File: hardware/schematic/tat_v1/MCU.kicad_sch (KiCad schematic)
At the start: 23 parts, among them J3 JST-SH 1x7P, SW2 SW_SPDT, SW3 SW_Push, U4 STM32U073CCUx, X1 32.768KHz

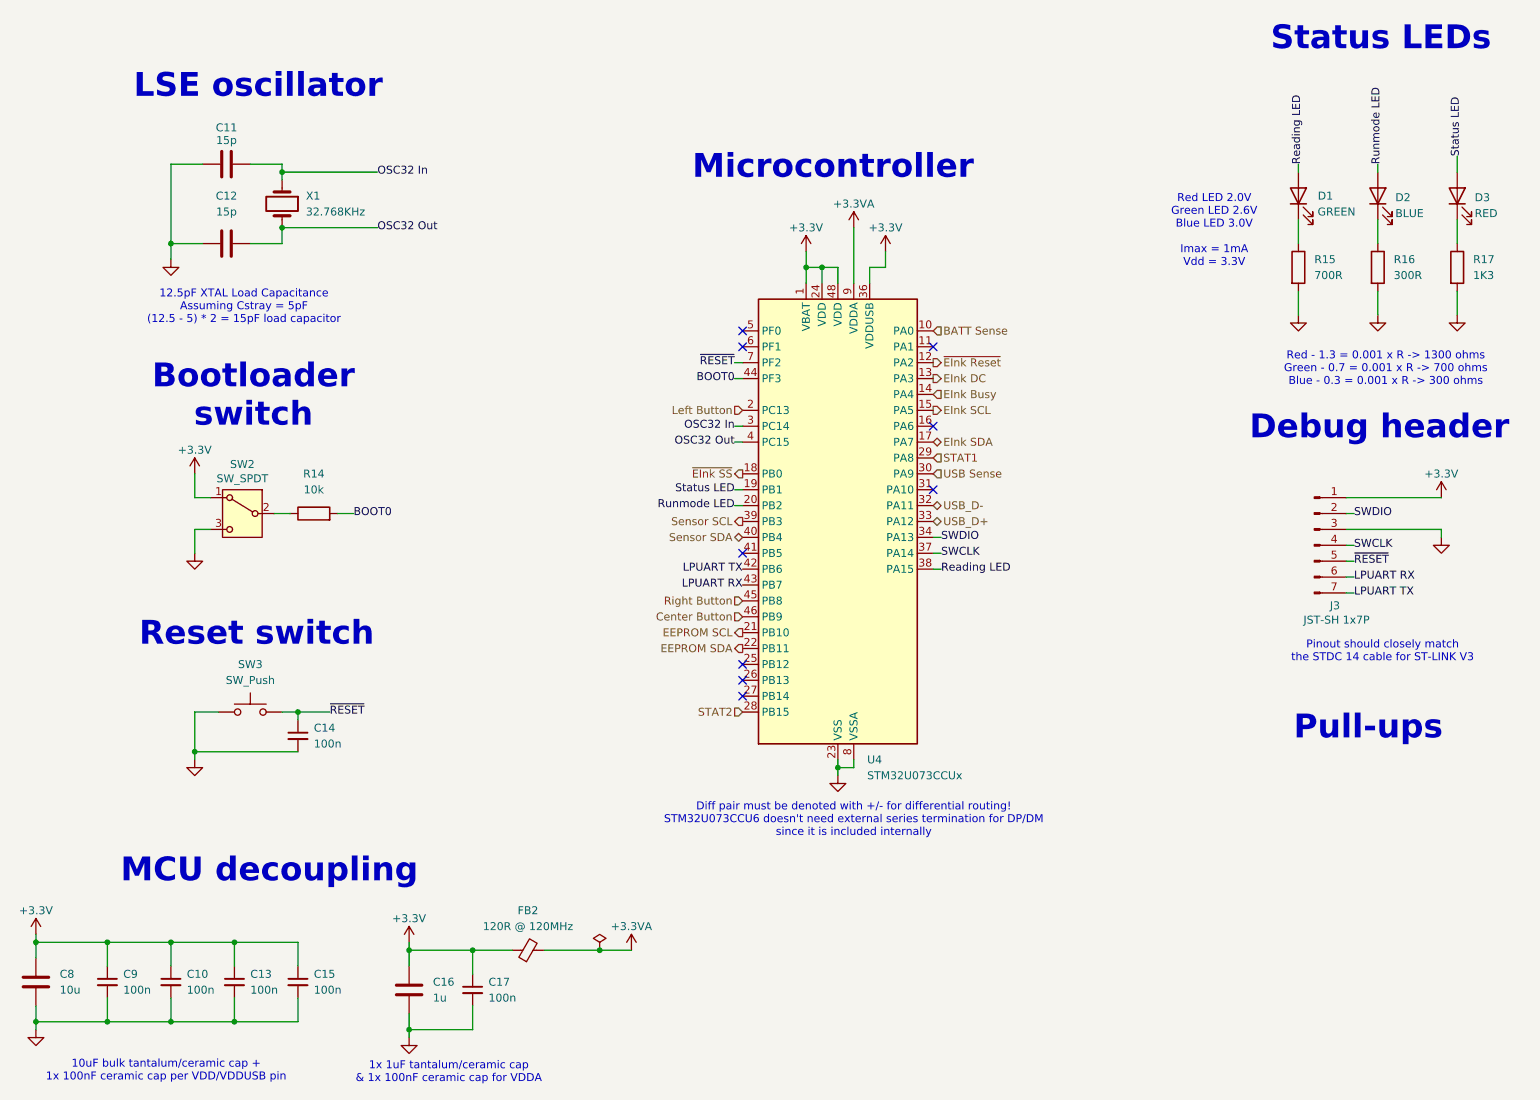
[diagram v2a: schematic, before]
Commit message: Most simple footprints added. Need to create footprints for more complex parts.
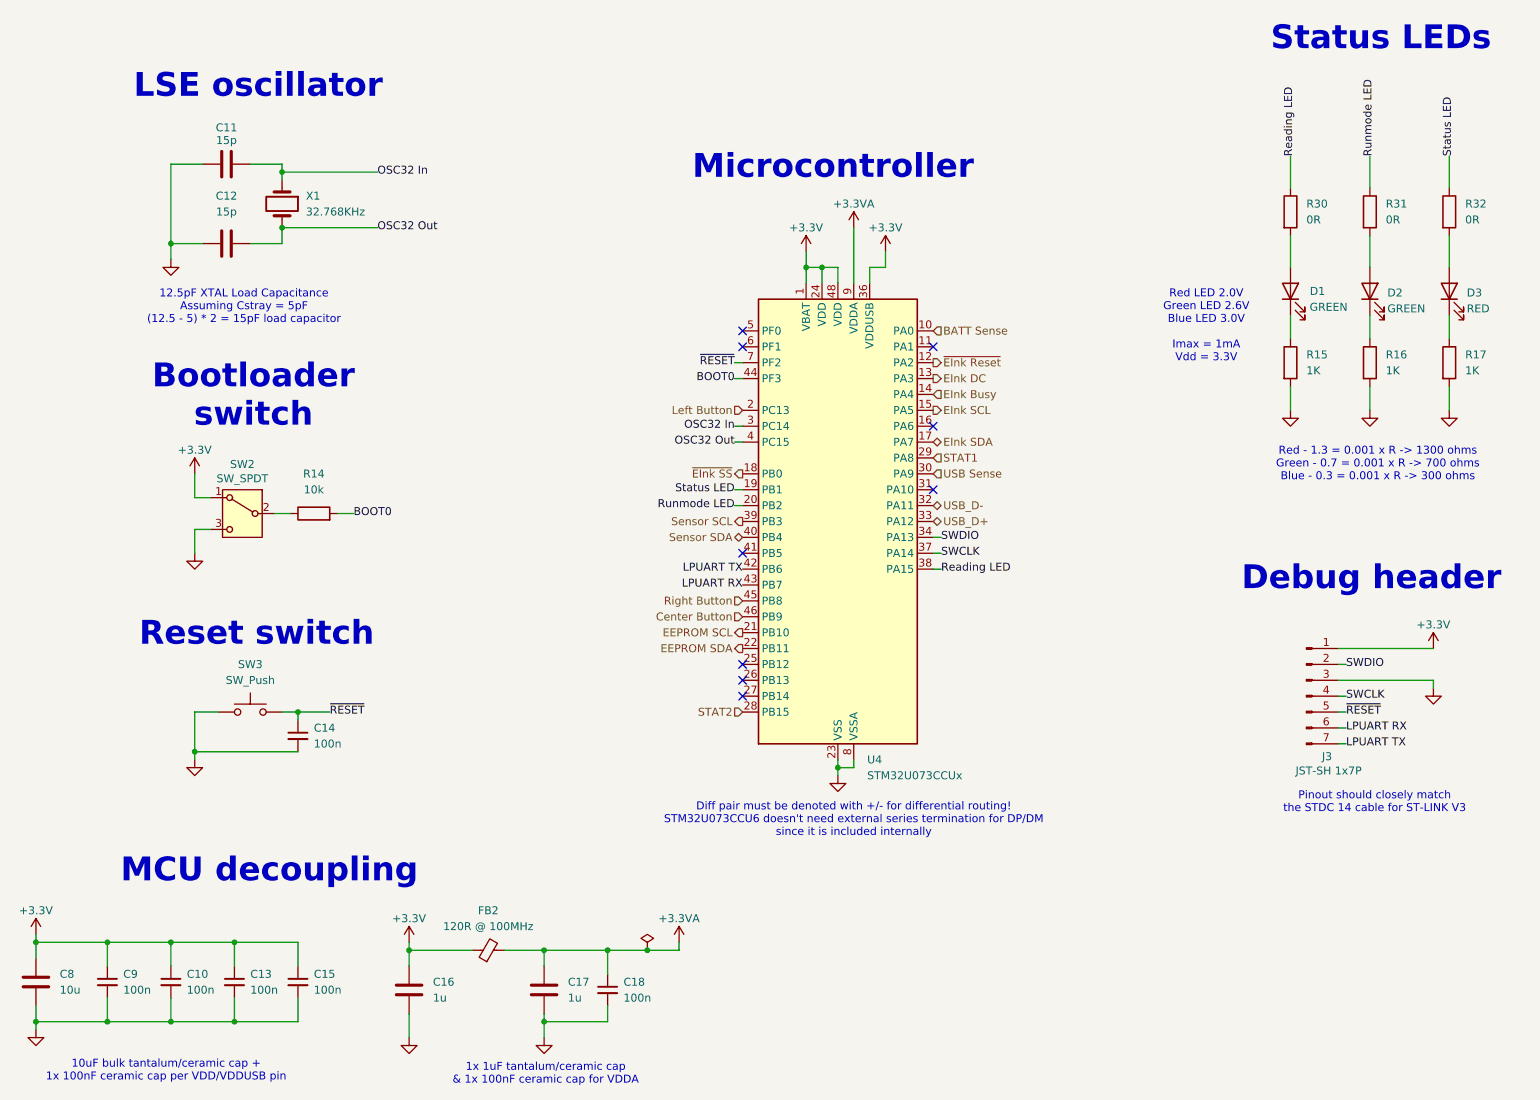
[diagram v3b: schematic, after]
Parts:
- added C16: 1u, symbol Device:C
- added R30, R31, R32: 0R, Jumper:SolderJumper-2_P1.3mm_Bridged2Bar_RoundedPad1.0x1.5mm, symbol Device:R
- C10, C11, C12, C13, C14, C15, C8, C9: Link (none) -> https://www.lcsc.com/product-detail/Multilayer-Ceramic-Capa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
- C17: renamed from C16; Link (none) -> https://www.lcsc.com/product-detail/Multilayer-Ceramic-Capa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
- C18: renamed from C17; Link (none) -> https://www.lcsc.com/product-detail/Multilayer-Ceramic-Capa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
- D1, D3: footprint (none) -> LED_SMD:LED_0603_1608Metric; Link (none) -> https://www.lcsc.com/product-detail/LED-Indication-Discrete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
- D2: value BLUE -> GREEN; footprint (none) -> LED_SMD:LED_0603_1608Metric; Link (none) -> https://www.lcsc.com/product-detail/LED-Indication-Discrete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
- FB2: value 120R @ 120MHz -> 120R @ 100MHz; footprint (none) -> Inductor_SMD:L_0603_1608Metric; Link (none) -> https://www.lcsc.com/product-detail/Ferrite-Beads_Murata-El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
- J3: footprint (none) -> Connector_JST:JST_SH_SM07B-SRSS-TB_1x07-1MP_P1.00mm_Horizontal; Link (none) -> https://www.lcsc.com/product-detail/Wire-To-Board-Connector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
- R15: value 700R -> 1K; footprint Resistor_SMD:R_0402_1005Metric -> Resistor_SMD:R_0603_1608Metric; Link (none) -> https://www.lcsc.com/product-detail/Chip-Resistor-Surface-M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
- R16: value 300R -> 1K; footprint Resistor_SMD:R_0402_1005Metric -> Resistor_SMD:R_0603_1608Metric; Link (none) -> https://www.lcsc.com/product-detail/Chip-Resistor-Surface-M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
- R17: value 1K3 -> 1K; footprint Resistor_SMD:R_0402_1005Metric -> Resistor_SMD:R_0603_1608Metric; Link (none) -> https://www.lcsc.com/product-detail/Chip-Resistor-Surface-M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
- SW3: footprint (none) -> Button_Switch_SMD:SW_Push_1P1T_XKB_TS-1187A
- X1: footprint (none) -> Crystal:Crystal_SMD_3215-2Pin_3.2x1.5mm; Link (none) -> https://www.lcsc.com/product-detail/Crystals_Seiko-Epson-Q1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
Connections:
- net +3.3V: now also C16.1; no longer C17.1, C18.1
- net +3.3VA: now also C17.1, C18.1
- net GND: now also C16.2
- net Reading LED: now also R30.1; no longer D1.2 (A)
- net Runmode LED: now also R31.1; no longer D2.2 (A)
- net Status LED: now also R32.1; no longer D3.2 (A)
- new net: D3.2 (A), R32.2
- new net: D2.2 (A), R31.2
- new net: D1.2 (A), R30.2
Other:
- note removed: "Pull-ups"
- moved on the sheet: C17, C18, D1, D2, D3, FB2, J3, R15, R16, R17

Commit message: Finished all footprints, can now start laying out circuit
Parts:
- C10, C13, C15, C18, C9: footprint (none) -> Capacitor_SMD:C_0402_1005Metric
- C16, C17: footprint (none) -> Capacitor_SMD:C_0603_1608Metric
- C8: footprint (none) -> Capacitor_SMD:C_0805_2012Metric
- SW2: footprint (none) -> tat_footprints:SW_SPDT_HANXIA_Mini_MSK12CO2
- SW3: footprint Button_Switch_SMD:SW_Push_1P1T_XKB_TS-1187A -> tat_footprints:SW_Push_SHOU_HAN_SPST_TS3425BA; Link (none) -> https://www.lcsc.com/product-detail/Tactile-Switches_XUNPU-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
- renumbered R30 to R15, R15 to R16, R31 to R17, R16 to R18, R32 to R19, R17 to R20
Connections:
- net +3.3V: now also SW2.3 (C); no longer SW2.1 (A)
- net GND: now also SW2.1 (A); no longer SW2.3 (C)
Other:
- moved on the sheet: SW2
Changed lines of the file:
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@@
 	(wire
 		(pts
-			(xy 50.8 93.98) (xy 53.34 93.98)
-		)
-		(stroke
-			(width 0)
-			(type default)
-		)
-	)
-	(wire
-		(pts
 			(xy 116.84 177.8) (xy 106.68 177.8)
 		)
@@
 	(wire
 		(pts
+			(xy 63.5 96.52) (xy 66.04 96.52)
+		)
+		(stroke
+			(width 0)
+			(type default)
+		)
+	)
+	(wire
+		(pts
 			(xy 251.46 76.2) (xy 251.46 80.01)
 		)
@@
 	(wire
 		(pts
+			(xy 50.8 93.98) (xy 53.34 93.98)
+		)
+		(stroke
+			(width 0)
+			(type default)
+		)
+	)
+	(wire
+		(pts
 			(xy 161.29 57.15) (xy 158.75 57.15)
 		)
@@
 	(wire
 		(pts
-			(xy 25.4 165.1) (xy 25.4 167.64)
+			(xy 50.8 99.06) (xy 53.34 99.06)
 		)
 		(stroke
@@
 	(wire
 		(pts
-			(xy 57.15 173.99) (xy 57.15 177.8)
-		)
-		(stroke
-			(width 0)
-			(type default)
-		)
-	)
-	(wire
-		(pts
-			(xy 233.68 130.81) (xy 234.95 130.81)
+			(xy 25.4 165.1) (xy 25.4 167.64)
 		)
 		(stroke
@@
 	(wire
 		(pts
-			(xy 170.18 102.87) (xy 168.91 102.87)
+			(xy 57.15 173.99) (xy 57.15 177.8)
 		)
 		(stroke
@@
 	(wire
 		(pts
-			(xy 25.4 163.83) (xy 25.4 165.1)
+			(xy 233.68 130.81) (xy 234.95 130.81)
 		)
 		(stroke
@@
 	(wire
 		(pts
-			(xy 85.09 165.1) (xy 85.09 166.37)
+			(xy 170.18 102.87) (xy 168.91 102.87)
 		)
 		(stroke
@@
 	(wire
 		(pts
-			(xy 50.8 90.17) (xy 50.8 93.98)
+			(xy 25.4 163.83) (xy 25.4 165.1)
 		)
 		(stroke
@@
 	(wire
 		(pts
-			(xy 53.34 99.06) (xy 50.8 99.06)
+			(xy 85.09 165.1) (xy 85.09 166.37)
 		)
 		(stroke
@@
 	(wire
 		(pts
-			(xy 63.5 96.52) (xy 66.04 96.52)
+			(xy 50.8 90.17) (xy 50.8 93.98)
 		)
 		(stroke
@@
 			)
 		)
-		(property "Footprint" ""
+		(property "Footprint" "Capacitor_SMD:C_0402_1005Metric"
 			(at 116.84 172.72 0)
 			(effects
@@
 	(symbol
 		(lib_id "Switch:SW_SPDT")
-		(at 58.42 96.52 0)
-		(mirror y)
+		(at 58.42 96.52 180)
 		(unit 1)
 		(exclude_from_sim no)
@@
 		(dnp no)
 		(property "Reference" "SW2"
-			(at 58.42 88.646 0)
+			(at 58.42 104.394 0)
 			(effects
 				(font
@@
 		)
 		(property "Value" "SW_SPDT"
-			(at 58.42 90.932 0)
+			(at 58.42 102.108 0)
 			(effects
 				(font
@@
 			)
 		)
-		(property "Footprint" ""
+		(property "Footprint" "tat_footprints:SW_SPDT_HANXIA_Mini_MSK12CO2"
 			(at 58.42 96.52 0)
 			(effects
@@
 		)
 		(property "Datasheet" "~"
-			(at 58.42 104.14 0)
+			(at 58.42 88.9 0)
 			(effects
 				(font
@@
 		(dnp no)
 		(fields_autoplaced yes)
-		(property "Reference" "R15"
+		(property "Reference" "R16"
 			(at 228.6 71.1199 0)
 			(effects
@@
 			(project "tat_v1"
 				(path "/b6d2ddf1-6792-45dd-afc9-29fd74d587ec/61278459-0872-433c-8091-dd4d841ee895"
-					(reference "R15")
+					(reference "R16")
 					(unit 1)
 				)
@@
 			)
 		)
-		(property "Footprint" ""
+		(property "Footprint" "Capacitor_SMD:C_0805_2012Metric"
 			(at 26.3652 175.26 0)
 			(effects
@@
 			)
 		)
-		(property "Footprint" ""
+		(property "Footprint" "Capacitor_SMD:C_0402_1005Metric"
 			(at 67.31 171.45 0)
 			(effects
@@
 			)
 		)
-		(property "Footprint" "Button_Switch_SMD:SW_Push_1P1T_XKB_TS-1187A"
+		(property "Footprint" "tat_footprints:SW_Push_SHOU_HAN_SPST_TS3425BA"
 			(at 59.69 123.19 0)
 			(effects
@@
 			)
 		)
-		(property "Datasheet" "~"
+		(property "Datasheet" "https://www.lcsc.com/datasheet/lcsc_datasheet_2410121507_XUNPU-TS-1089S-02526_C455282.pdf"
 			(at 59.69 123.19 0)
 			(effects
@@
 			)
 		)
+		(property "Link" "https://www.lcsc.com/product-detail/Tactile-Switches_XUNPU-TS-1089S-02526_C455282.html"
+			(at 59.69 128.27 0)
+			(effects
+				(font
+					(size 1.27 1.27)
+				)
+				(hide yes)
+			)
+		)
 		(pin "2"
 		)
@@
 			)
 		)
-		(property "Footprint" ""
+		(property "Footprint" "Capacitor_SMD:C_0603_1608Metric"
 			(at 86.0552 176.53 0)
 			(effects
@@
 			)
 		)
-		(property "Footprint" ""
+		(property "Footprint" "Capacitor_SMD:C_0402_1005Metric"
 			(at 57.15 171.45 0)
 			(effects
@@
 		(dnp no)
 		(fields_autoplaced yes)
-		(property "Reference" "R31"
+		(property "Reference" "R17"
 			(at 241.3 46.9899 0)
 			(effects
@@
 			(project "tat_v1"
 				(path "/b6d2ddf1-6792-45dd-afc9-29fd74d587ec/61278459-0872-433c-8091-dd4d841ee895"
-					(reference "R31")
+					(reference "R17")
 					(unit 1)
 				)
@@
 		(dnp no)
 		(fields_autoplaced yes)
-		(property "Reference" "R17"
+		(property "Reference" "R20"
 			(at 254 71.1199 0)
 			(effects
@@
 			(project "tat_v1"
 				(path "/b6d2ddf1-6792-45dd-afc9-29fd74d587ec/61278459-0872-433c-8091-dd4d841ee895"
-					(reference "R17")
+					(reference "R20")
 					(unit 1)
 				)
@@
 			)
 		)
-		(property "Footprint" ""
+		(property "Footprint" "Capacitor_SMD:C_0603_1608Metric"
 			(at 107.6452 176.53 0)
 			(effects
@@
 		(dnp no)
 		(fields_autoplaced yes)
-		(property "Reference" "R16"
+		(property "Reference" "R18"
 			(at 241.3 71.1199 0)
 			(effects
@@
 			(project "tat_v1"
 				(path "/b6d2ddf1-6792-45dd-afc9-29fd74d587ec/61278459-0872-433c-8091-dd4d841ee895"
-					(reference "R16")
+					(reference "R18")
 					(unit 1)
 				)
@@
 			)
 		)
-		(property "Footprint" ""
+		(property "Footprint" "Capacitor_SMD:C_0402_1005Metric"
 			(at 36.83 171.45 0)
 			(effects
@@
 		(dnp no)
 		(fields_autoplaced yes)
-		(property "Reference" "R30"
+		(property "Reference" "R15"
 			(at 228.6 46.9899 0)
 			(effects
@@
 			(project ""
 				(path "/b6d2ddf1-6792-45dd-afc9-29fd74d587ec/61278459-0872-433c-8091-dd4d841ee895"
-					(reference "R30")
+					(reference "R15")
 					(unit 1)
 				)
@@
 		(dnp no)
 		(fields_autoplaced yes)
-		(property "Reference" "R32"
+		(property "Reference" "R19"
 			(at 254 46.9899 0)
 			(effects
@@
 			(project "tat_v1"
 				(path "/b6d2ddf1-6792-45dd-afc9-29fd74d587ec/61278459-0872-433c-8091-dd4d841ee895"
-					(reference "R32")
+					(reference "R19")
 					(unit 1)
 				)
@@
 			)
 		)
-		(property "Footprint" ""
+		(property "Footprint" "Capacitor_SMD:C_0402_1005Metric"
 			(at 46.99 171.45 0)
 			(effects

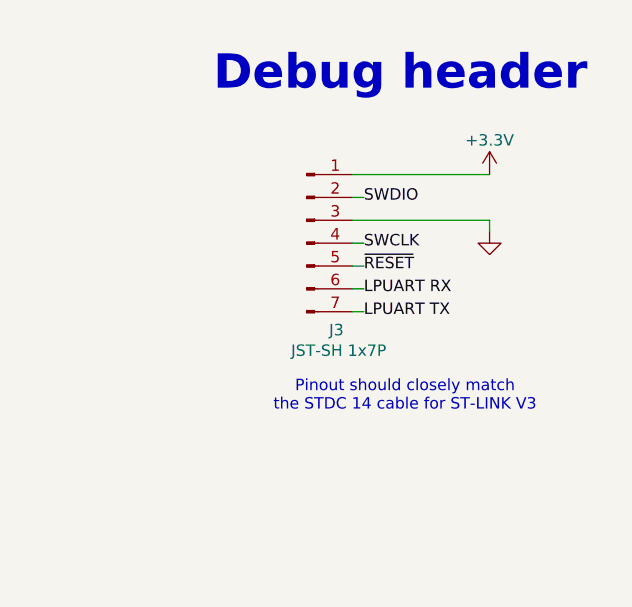
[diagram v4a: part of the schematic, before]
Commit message: Fixed all footprint-symbol mismatches, ready to start routing!
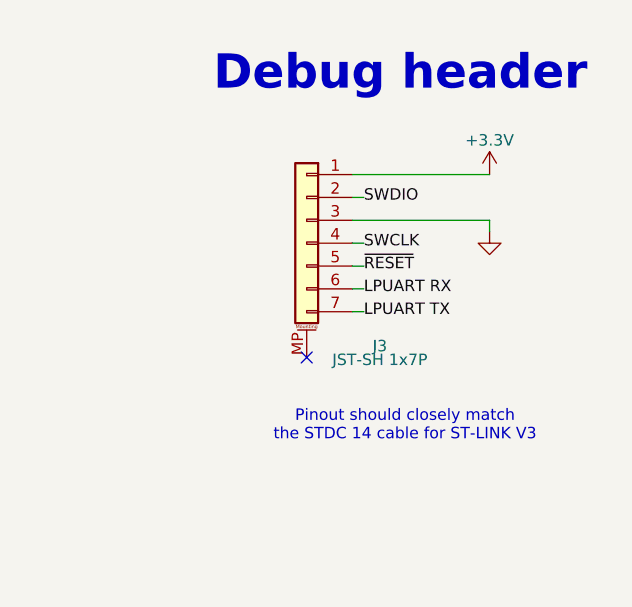
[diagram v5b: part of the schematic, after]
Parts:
- J3: symbol Connector:Conn_01x07_Pin -> Connector_Generic_MountingPin:Conn_01x07_MountingPin
- SW2: symbol Switch:SW_SPDT -> tat_library:MINI_MSK12CO2; Link (none) -> https://www.lcsc.com/product-detail/Slide-Switches_SHOU-HAN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
- SW3: footprint tat_footprints:SW_Push_SHOU_HAN_SPST_TS3425BA -> tat_footprints:SW_Push_SHOU_HAN_SPST_RightAngle_TS24CA; symbol Switch:SW_Push -> tat_library:TS24CA; Link https://www.lcsc.com/product-detail/Tactile-Switches_XUNPU-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 -> https://www.lcsc.com/product-detail/Tactile-Switches_SHOU-H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
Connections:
- no-connect marks 9 -> 10
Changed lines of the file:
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@@
 	(text "Pinout should closely match \nthe STDC 14 cable for ST-LINK V3"
 		(exclude_from_sim no)
-		(at 239.522 142.748 0)
+		(at 239.522 146.05 0)
 		(effects
 			(font
@@
 	(no_connect
 		(at 168.91 82.55)
+	)
+	(no_connect
+		(at 228.6 138.43)
 	)
 	(no_connect
@@
 	)
 	(symbol
-		(lib_id "Switch:SW_SPDT")
+		(lib_id "tat_library:MINI_MSK12CO2")
 		(at 58.42 96.52 180)
 		(unit 1)
@@
 			)
 		)
-		(property "Datasheet" "~"
-			(at 58.42 88.9 0)
+		(property "Datasheet" "https://www.lcsc.com/datasheet/lcsc_datasheet_2407161403_SHOU-HAN-MINI-MSK12CO2_C2681570.pdf"
+			(at 58.42 88.646 0)
 			(effects
 				(font
@@
 			)
 		)
+		(property "Link" "https://www.lcsc.com/product-detail/Slide-Switches_SHOU-HAN-MINI-MSK12CO2_C2681570.html?s_z=n_SHOU%2520HAN%2520MINI%2520MSK12CO2"
+			(at 58.42 96.52 0)
+			(effects
+				(font
+					(size 1.27 1.27)
+				)
+				(hide yes)
+			)
+		)
 		(pin "3"
 		)
@@
 		)
 		(pin "2"
+		)
+		(pin "6"
+		)
+		(pin "4"
+		)
+		(pin "5"
+		)
+		(pin "7"
 		)
 		(instances
@@
 	)
 	(symbol
-		(lib_id "Switch:SW_Push")
+		(lib_id "tat_library:TS24CA")
 		(at 59.69 128.27 0)
 		(unit 1)
@@
 			)
 		)
-		(property "Footprint" "tat_footprints:SW_Push_SHOU_HAN_SPST_TS3425BA"
+		(property "Footprint" "tat_footprints:SW_Push_SHOU_HAN_SPST_RightAngle_TS24CA"
 			(at 59.69 123.19 0)
 			(effects
@@
 			)
 		)
-		(property "Datasheet" "https://www.lcsc.com/datasheet/lcsc_datasheet_2410121507_XUNPU-TS-1089S-02526_C455282.pdf"
+		(property "Datasheet" "https://www.lcsc.com/datasheet/lcsc_datasheet_2404241539_SHOU-HAN-TS24CA_C393942.pdf"
 			(at 59.69 123.19 0)
 			(effects
@@
 			)
 		)
-		(property "Link" "https://www.lcsc.com/product-detail/Tactile-Switches_XUNPU-TS-1089S-02526_C455282.html"
+		(property "Link" "https://www.lcsc.com/product-detail/Tactile-Switches_SHOU-HAN-TS24CA_C393942.html?s_z=n_SHOU%2520HAN%2520TS24CA"
 			(at 59.69 128.27 0)
 			(effects
@@
 		)
 		(pin "1"
+		)
+		(pin "3"
+		)
+		(pin "4"
 		)
 		(instances
@@
 	)
 	(symbol
-		(lib_id "Connector:Conn_01x07_Pin")
+		(lib_id "Connector_Generic_MountingPin:Conn_01x07_MountingPin")
 		(at 228.6 125.73 0)
+		(mirror y)
 		(unit 1)
 		(exclude_from_sim no)
@@
 		(dnp no)
 		(property "Reference" "J3"
-			(at 231.902 135.382 0)
+			(at 236.728 137.16 0)
 			(effects
 				(font
@@
 		)
 		(property "Value" "JST-SH 1x7P"
-			(at 232.156 137.668 0)
+			(at 236.728 138.684 0)
 			(effects
 				(font
@@
 			)
 		)
-		(property "Datasheet" "https://www.lcsc.com/datasheet/lcsc_datasheet_2304140030_JST-SM07B-SRSS-TB-LF-SN_C160406.pdf"
+		(property "Datasheet" "~"
 			(at 228.6 125.73 0)
 			(effects
@@
 			)
 		)
-		(property "Description" "JST-SH 7-pin header"
+		(property "Description" "Generic connectable mounting pin connector, single row, 01x07, script generated (kicad-library-utils/schlib/autogen/connector/)"
 			(at 228.6 125.73 0)
 			(effects
@@
 		(pin "2"
 		)
+		(pin "MP"
+		)
 		(instances
